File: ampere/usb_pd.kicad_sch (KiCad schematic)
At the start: 59 parts, among them Q2 CSD25480F3, Q3 CSD25480F3, Q4 CSD15380F3, Q5 CSD15380F3, Q6 CSD15380F3, Q7 CSD15380F3, Q8 CSD18543Q3A, U3 TPS26750SRSMR, U4 TPD4S480RUKR, U5 CAT24C256

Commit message: add LDOs, 90 percent of TPS55289s
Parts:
- Q2, Q3: value CSD25480F3 -> CSD25481F4; footprint Package_DFN_QFN:Texas_PicoStar_DFN-3_0.69x0.60mm -> CSD25481F4:TRANS_CSD25481F4
- Q4, Q5, Q6, Q7: value CSD15380F3 -> CSD13381F4; footprint Package_DFN_QFN:Texas_PicoStar_DFN-3_0.69x0.60mm -> CSD13381F4:DFN100X60X35-3N
- R10, R11, R8, R9: now not fitted
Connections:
- net ADCIN1: no longer U3.2 (ADCIN1)
- net ADCIN2: no longer U3.3 (ADCIN2)
- net GND: now also U3.2 (ADCIN1), U3.3 (ADCIN2)

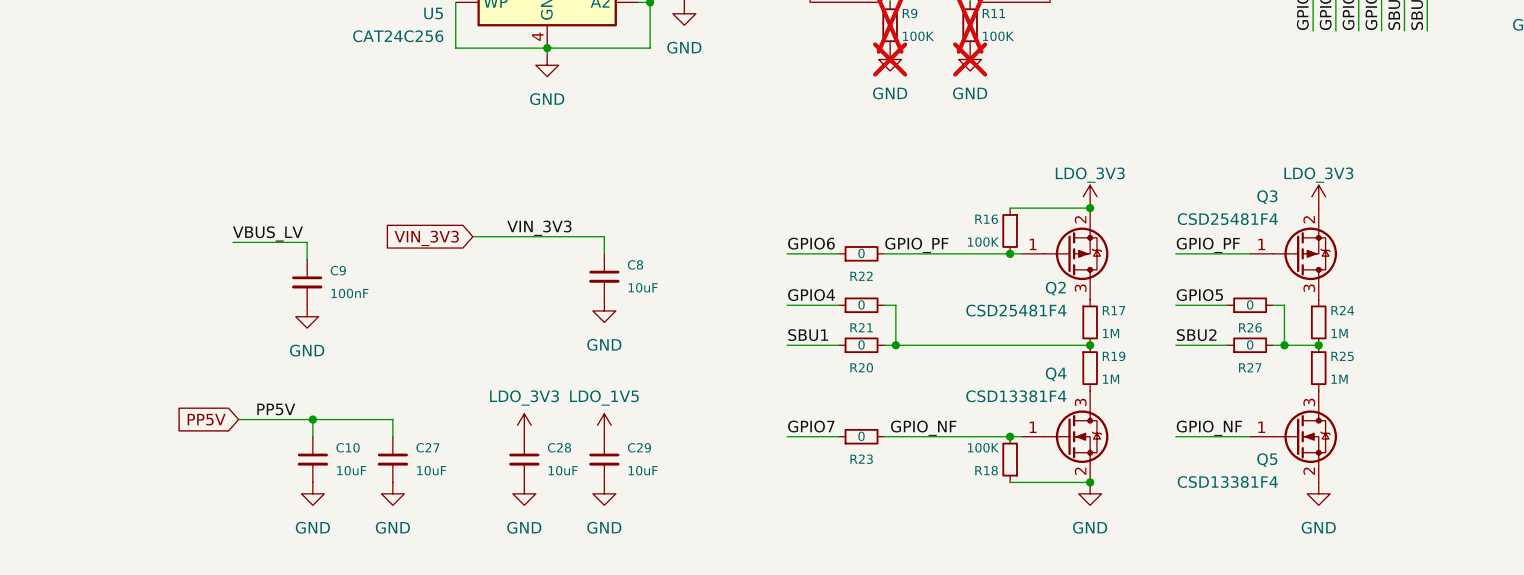
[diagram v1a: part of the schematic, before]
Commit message: make more room for the load switch thingy
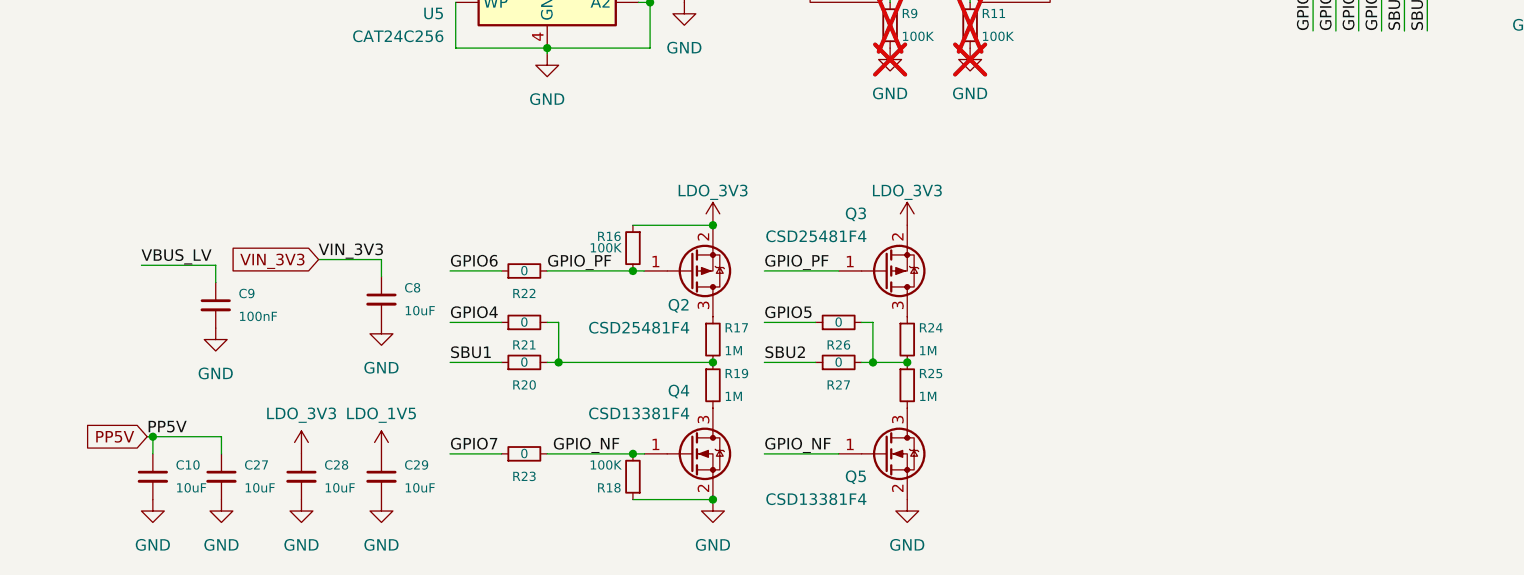
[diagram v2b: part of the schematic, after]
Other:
- moved on the sheet: C10, C27, C28, C29, C8, C9, Q2, Q3, Q4, Q5, R16, R17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

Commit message: update some footprints
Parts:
- added U21: LM74502DDFR, LM74502DDFR:SOT65P280X110-8N, symbol LM74502DDFR:LM74502DDFR
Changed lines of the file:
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@@
+	)
+	(symbol
+		(lib_id "LM74502DDFR:LM74502DDFR")
+		(at 148.59 167.64 0)
+		(unit 1)
+		(body_style 1)
+		(exclude_from_sim no)
+		(in_bom yes)
+		(on_board yes)
+		(in_pos_files yes)
+		(dnp no)
+		(fields_autoplaced yes)
+		(property "Reference" "U21"
+			(at 148.59 149.86 0)
+			(show_name no)
+			(do_not_autoplace no)
+			(effects
+				(font
+					(size 1.27 1.27)
+				)
+			)
+		)
+		(property "Value" "LM74502DDFR"
+			(at 148.59 152.4 0)
+			(show_name no)
+			(do_not_autoplace no)
+			(effects
+				(font
+					(size 1.27 1.27)
+				)
+			)
+		)
+		(property "Footprint" "LM74502DDFR:SOT65P280X110-8N"
+			(at 148.59 167.64 0)
+			(hide yes)
+			(show_name no)
+			(do_not_autoplace no)
+			(effects
+				(font
+					(size 1.27 1.27)
+				)
+				(justify bottom)
+			)
+		)
+		(property "Datasheet" ""
+			(at 148.59 167.64 0)
+			(hide yes)
+			(show_name no)
+			(do_not_autoplace no)
+			(effects
+				(font
+					(size 1.27 1.27)
+				)
+			)
+		)
+		(property "Description" ""
+			(at 148.59 167.64 0)
+			(hide yes)
+			(show_name no)
+			(do_not_autoplace no)
+			(effects
+				(font
+					(size 1.27 1.27)
+				)
+			)
+		)
+		(property "MAXIMUM_PACKAGE_HEIGHT" "1.1mm"
+			(at 148.59 167.64 0)
+			(hide yes)
+			(show_name no)
+			(do_not_autoplace no)
+			(effects
+				(font
+					(size 1.27 1.27)
+				)
+				(justify bottom)
+			)
+		)
+		(property "CREATOR" "ASHISH"
+			(at 148.59 167.64 0)
+			(hide yes)
+			(show_name no)
+			(do_not_autoplace no)
+			(effects
+				(font
+					(size 1.27 1.27)
+				)
+				(justify bottom)
+			)
+		)
+		(property "NOTES" ""
+			(at 148.59 167.64 0)
+			(hide yes)
+			(show_name no)
+			(do_not_autoplace no)
+			(effects
+				(font
+					(size 1.27 1.27)
+				)
+				(justify bottom)
+			)
+		)
+		(property "STANDARD" "IPC-7351B"
+			(at 148.59 167.64 0)
+			(hide yes)
+			(show_name no)
+			(do_not_autoplace no)
+			(effects
+				(font
+					(size 1.27 1.27)
+				)
+				(justify bottom)
+			)
+		)
+		(property "PARTREV" "A"
+			(at 148.59 167.64 0)
+			(hide yes)
+			(show_name no)
+			(do_not_autoplace no)
+			(effects
+				(font
+					(size 1.27 1.27)
+				)
+				(justify bottom)
+			)
+		)
+		(property "VERIFIER" ""
+			(at 148.59 167.64 0)
+			(hide yes)
+			(show_name no)
+			(do_not_autoplace no)
+			(effects
+				(font
+					(size 1.27 1.27)
+				)
+				(justify bottom)
+			)
+		)
+		(property "UNIT" "mm"
+			(at 148.59 167.64 0)
+			(hide yes)
+			(show_name no)
+			(do_not_autoplace no)
+			(effects
+				(font
+					(size 1.27 1.27)
+				)
+				(justify bottom)
+			)
+		)
+		(property "MANUFACTURER" "Texas Instruments"
+			(at 148.59 167.64 0)
+			(hide yes)
+			(show_name no)
+			(do_not_autoplace no)
+			(effects
+				(font
+					(size 1.27 1.27)
+				)
+				(justify bottom)
+			)
+		)
+		(pin "1"
+		)
+		(pin "7"
+		)
+		(pin "3"
+		)
+		(pin "8"
+		)
+		(pin "4"
+		)
+		(pin "6"
+		)
+		(pin "2"
+		)
+		(pin "5"
+		)
+		(instances
+			(project "ampere"
+				(path "/8a6a9ad3-5df1-4e31-824c-811a1f6dd084"
+					(reference "U21")
+					(unit 1)
+				)
+			)
+		)
 	)
 	(symbol

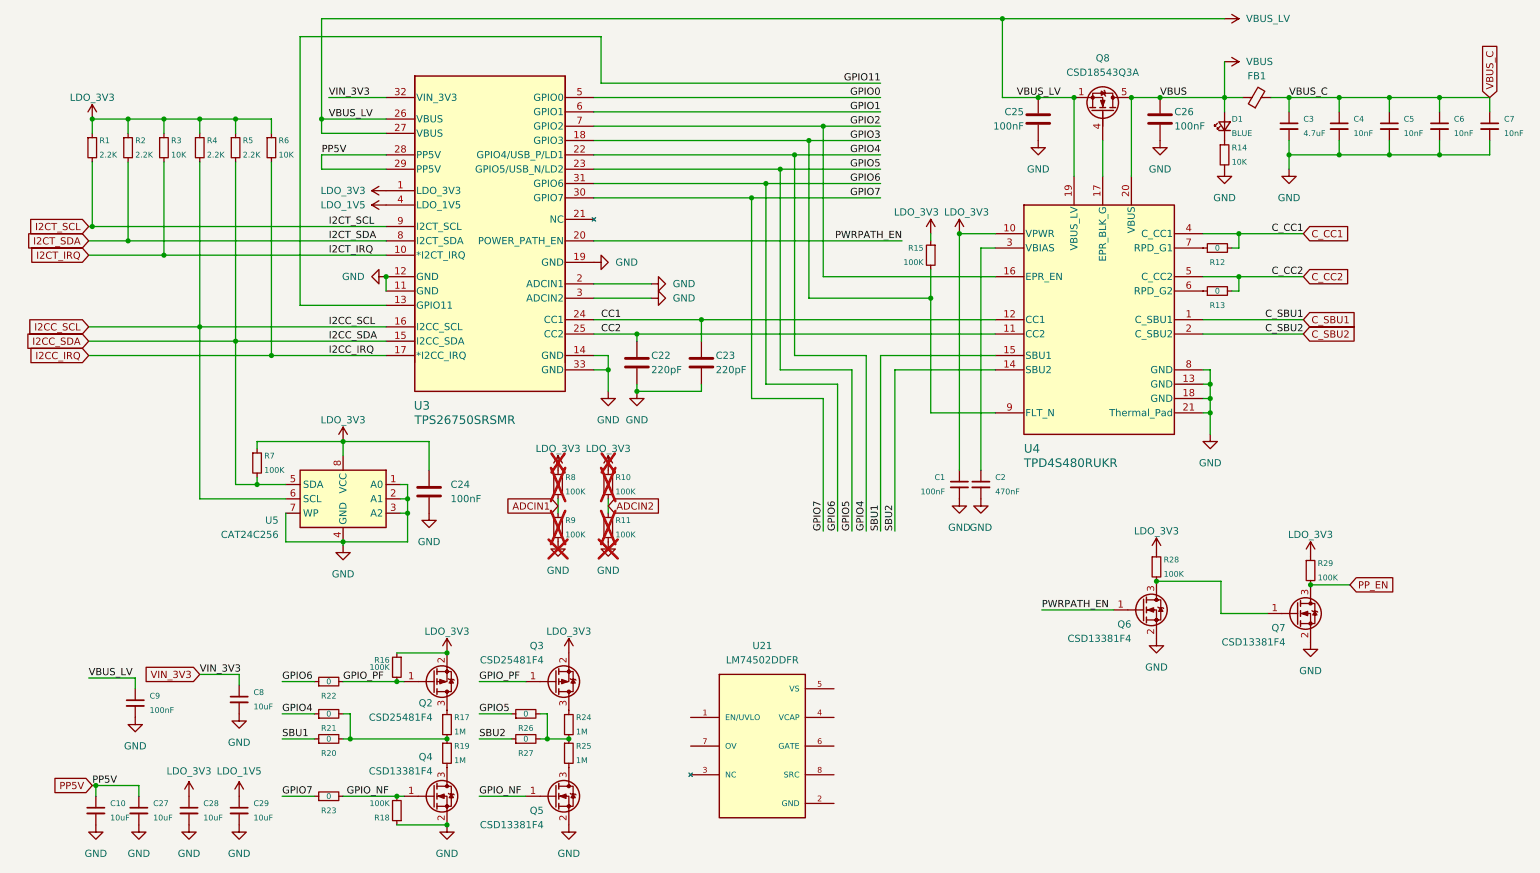
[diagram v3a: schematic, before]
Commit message: LM74502 implementation v1
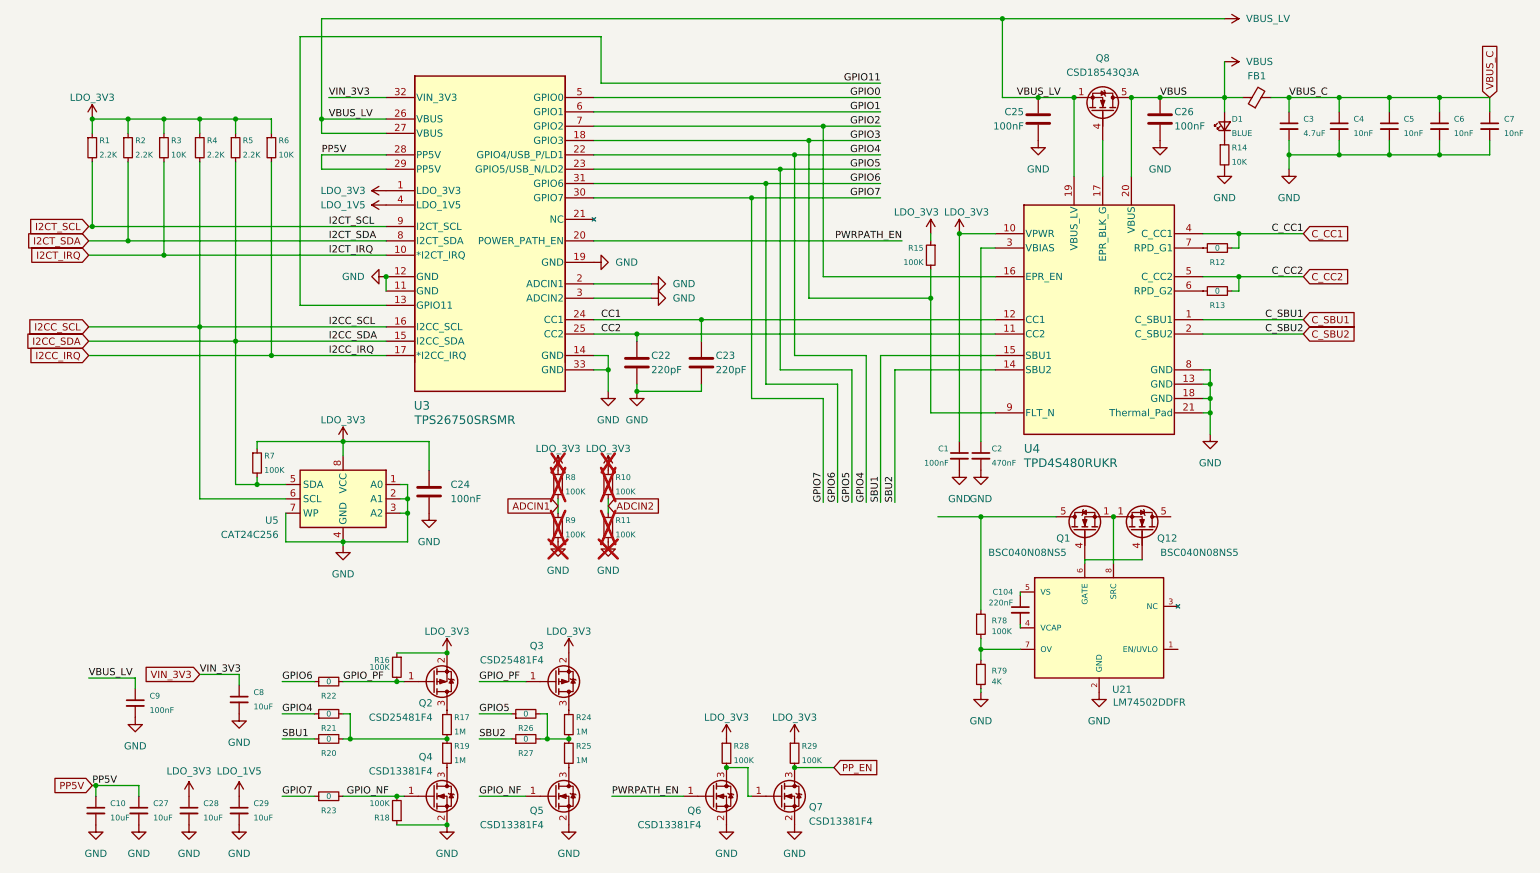
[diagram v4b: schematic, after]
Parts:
- added C104: 220nF, Capacitor_SMD:C_0402_1005Metric, symbol Device:C_Small
- added Q1, Q12: BSC040N08NS5, Package_TO_SOT_SMD:TDSON-8-1, symbol Transistor_FET:BSC040N08NS5
- added R78: 100K, Resistor_SMD:R_0603_1608Metric, symbol Device:R_Small
- added R79: 4K, Resistor_SMD:R_0603_1608Metric, symbol Device:R_Small
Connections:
- net GND: now also U21.2 (GND), R79.2
- net at U21.4 (VCAP): now also C104.2
- net at U21.5 (VS): now also C104.1
- net at U21.6 (GATE): now also Q1.4 (G), Q12.4 (G)
- net at U21.7 (OV): now also R78.2, R79.1
- net at U21.8 (SRC): now also Q1.1 (S), Q1.2 (S), Q1.3 (S), Q12.1 (S), Q12.2 (S), Q12.3 (S)
- new net: Q1.5 (D), R78.1
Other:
- moved on the sheet: C1, C2, Q6, Q7, R28, R29, U21

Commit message: upgrade the FETS for power path enable
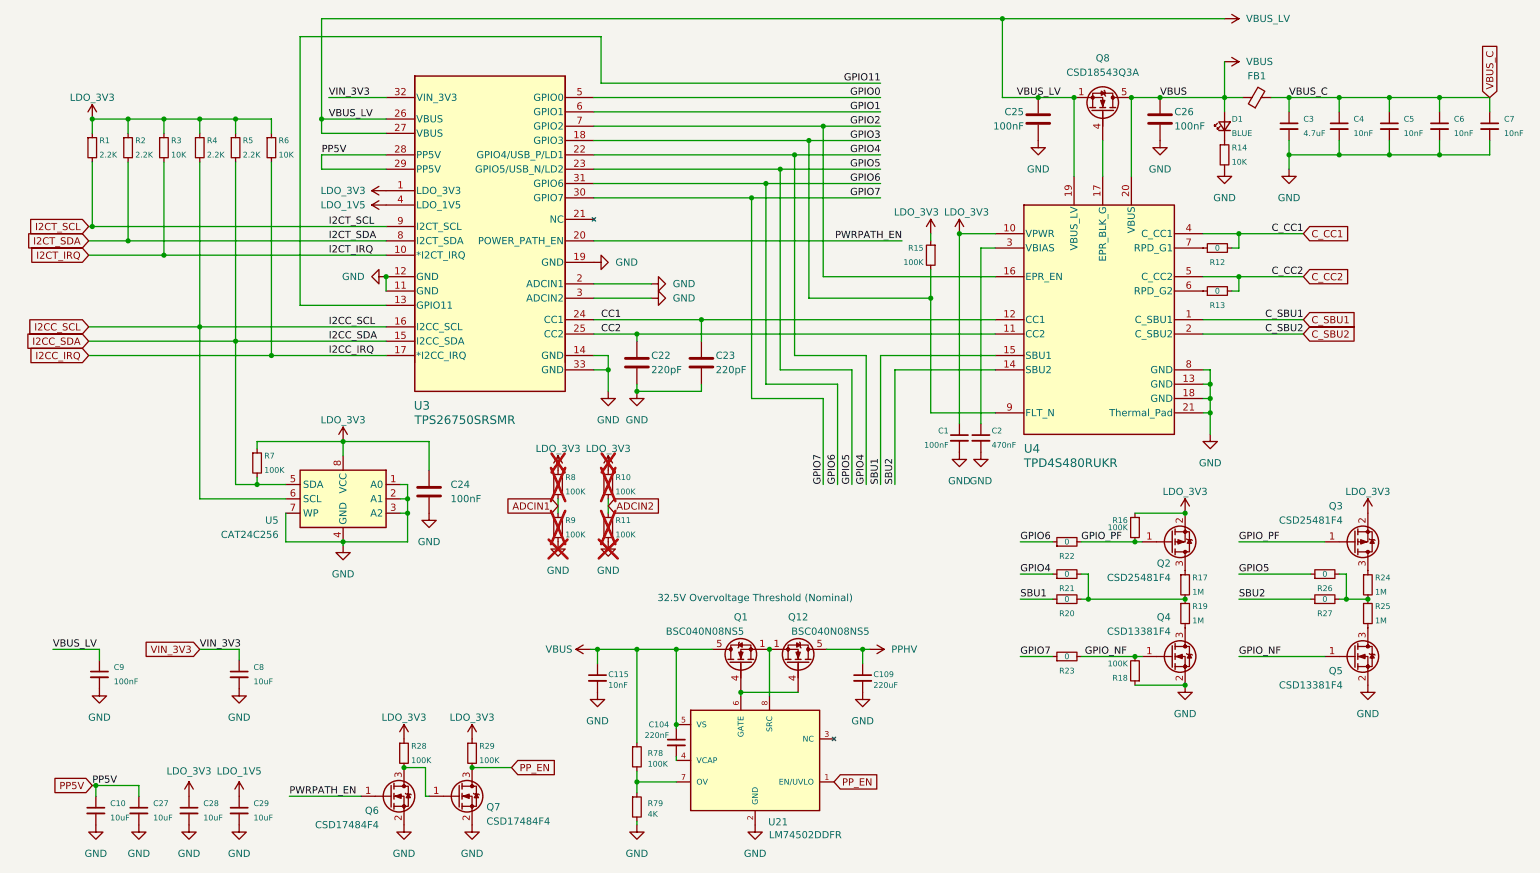
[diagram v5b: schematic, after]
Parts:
- added C109: 220uF, Capacitor_SMD:C_0402_1005Metric, symbol Device:C_Small
- added C115: 10nF, Capacitor_SMD:C_0402_1005Metric, symbol Device:C_Small
- Q6, Q7: value CSD13381F4 -> CSD17484F4
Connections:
- net GND: now also C109.2, C115.2
- net PP_EN: now also U21.1 (EN/UVLO)
- net VBUS: now also C104.1, Q1.5 (D), R78.1, U21.5 (VS), C115.1
- net PPHV: now reaches Q12.5 (D)
- net PPHV: now also C109.1
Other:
- note added: "32.5V Overvoltage Threshold (Nominal)"
- moved on the sheet: C1, C104, C2, C8, C9, Q1, Q12, Q2, Q3, Q4, Q5, Q6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

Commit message: implement tps26750 and tpd4s480
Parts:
- C10, C27: footprint Capacitor_SMD:C_0402_1005Metric -> Capacitor_SMD:C_0603_1608Metric
- U4: footprint TPD4S480:RUK0020B-IPC_B -> TPD4S480:RUK0020B-MFG
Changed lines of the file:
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@@
 			)
 		)
-		(property "Footprint" "Capacitor_SMD:C_0402_1005Metric"
+		(property "Footprint" "Capacitor_SMD:C_0603_1608Metric"
 			(at 38.1 179.07 0)
 			(hide yes)
@@
 			)
 		)
-		(property "Footprint" "TPD4S480:RUK0020B-IPC_B"
+		(property "Footprint" "TPD4S480:RUK0020B-MFG"
 			(at 189.865 76.835 0)
 			(hide yes)
@@
 			)
 		)
-		(property "Footprint" "Capacitor_SMD:C_0402_1005Metric"
+		(property "Footprint" "Capacitor_SMD:C_0603_1608Metric"
 			(at 30.48 179.07 0)
 			(hide yes)

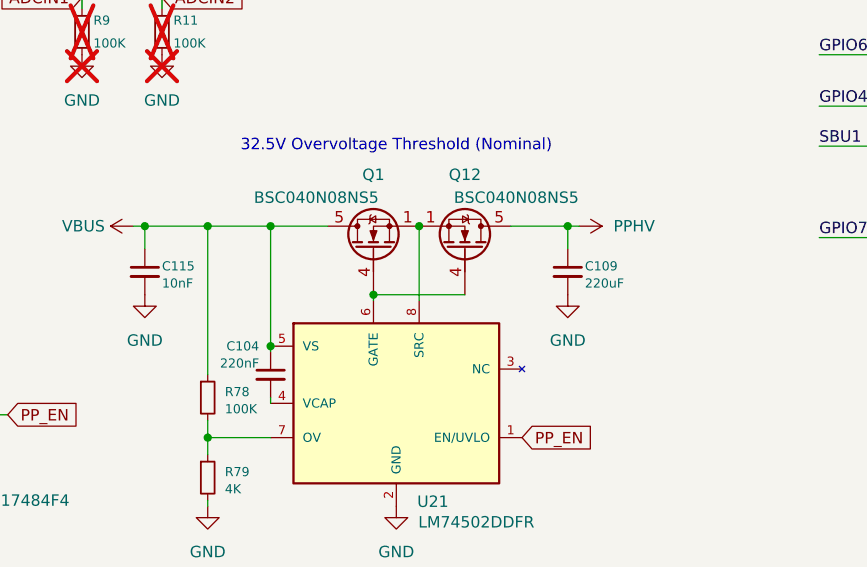
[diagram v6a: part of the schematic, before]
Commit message: layout and perform copper pours for lm74502
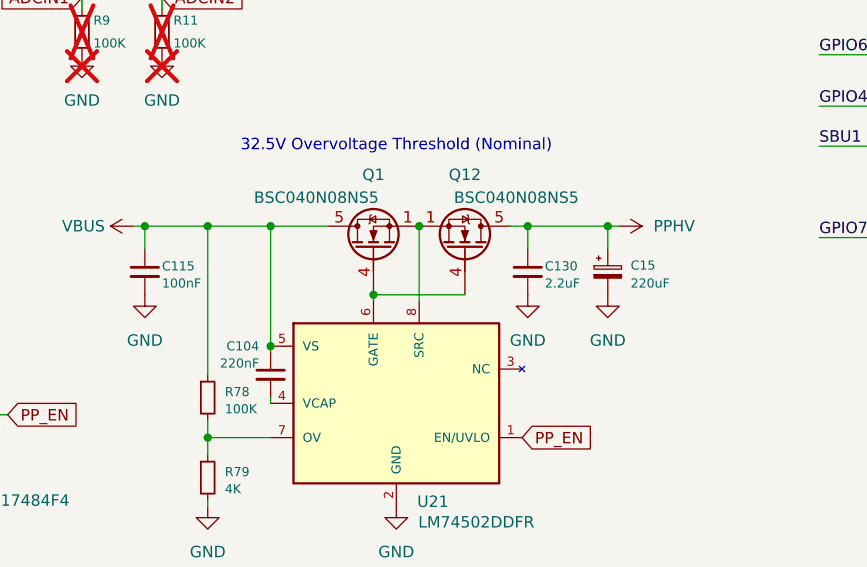
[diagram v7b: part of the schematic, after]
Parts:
- removed C109: 220uF, Capacitor_SMD:C_0402_1005Metric, symbol Device:C_Small
- added C130: 2.2uF, Capacitor_SMD:C_1210_3225Metric, symbol Device:C_Small
- added C15: 220uF, Capacitor_SMD:CP_Elec_10x10, symbol Device:C_Polarized_Small
- C104: footprint Capacitor_SMD:C_0402_1005Metric -> Capacitor_SMD:C_0603_1608Metric
- C115: value 10nF -> 100nF; footprint Capacitor_SMD:C_0402_1005Metric -> Capacitor_SMD:C_0603_1608Metric
- R78, R79: footprint Resistor_SMD:R_0603_1608Metric -> Resistor_SMD:R_0402_1005Metric
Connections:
- net GND: now also C130.2, C15.2
- net PPHV: now also C130.1, C15.1

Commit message: start blocking control portion
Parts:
- C15: footprint Capacitor_SMD:CP_Elec_10x10 -> Capacitor_SMD:CP_Elec_8x10
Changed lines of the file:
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@@
 			)
 		)
-		(property "Footprint" "Capacitor_SMD:CP_Elec_10x10"
+		(property "Footprint" "Capacitor_SMD:CP_Elec_8x10"
 			(at 170.815 155.575 0)
 			(hide yes)
